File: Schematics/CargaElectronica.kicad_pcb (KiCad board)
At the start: 2 copper layers, 88 x 78.2 mm, 46 parts, among them J1 Voltage_test, J2 Voltage_IN, Q1 IRFP460, SW1 Rotary_Encoder_Switch, SW2 Btn.OK, SW3 Btn.BCK, U1 TL072, U2 Pantalla_LCD_16x2_i2c, U3 LM35-LP, U4 TL431DBZ

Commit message: Modified PCB
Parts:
- added REF**: MountingHole_3.2mm_M3_ISO14580_Pad_TopBottom, MountingHole:MountingHole_3.2mm_M3_ISO14580_Pad_TopBottom, F.Cu at (178.5, 127.8)
- added REF**: MountingHole_3.2mm_M3_ISO14580_Pad_TopBottom, MountingHole:MountingHole_3.2mm_M3_ISO14580_Pad_TopBottom, F.Cu at (104.8, 127.5)
- added REF**: MountingHole_3.2mm_M3_ISO14580_Pad_TopBottom, MountingHole:MountingHole_3.2mm_M3_ISO14580_Pad_TopBottom, F.Cu at (178.8, 97.5)
- moved REF** 13.2 mm to (126.0, 123.2)
- moved G*** 12.6 mm to (163.5, 112.2)
- moved U2 3.75 mm to (104.0, 99.8)
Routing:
- net 5V: track 89.9 -> 53.9 mm
- net Net-(A1-Pad24): track 31.2 -> 0.00 mm
- net Net-(A1-Pad23): track 27.6 -> 0.00 mm
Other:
- board size 88 x 78.2 mm -> 88 x 94.2 mm

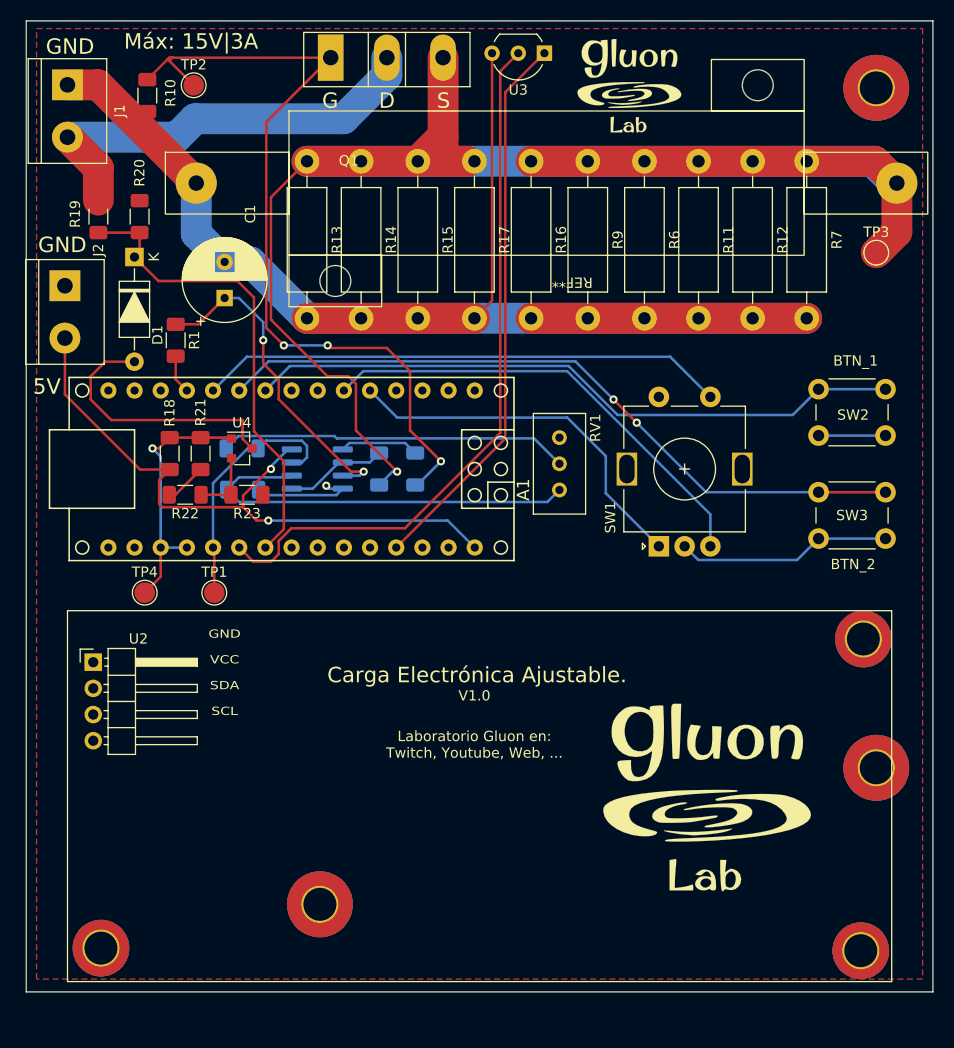
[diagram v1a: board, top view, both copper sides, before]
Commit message: Updated schematic, did not update with last commit
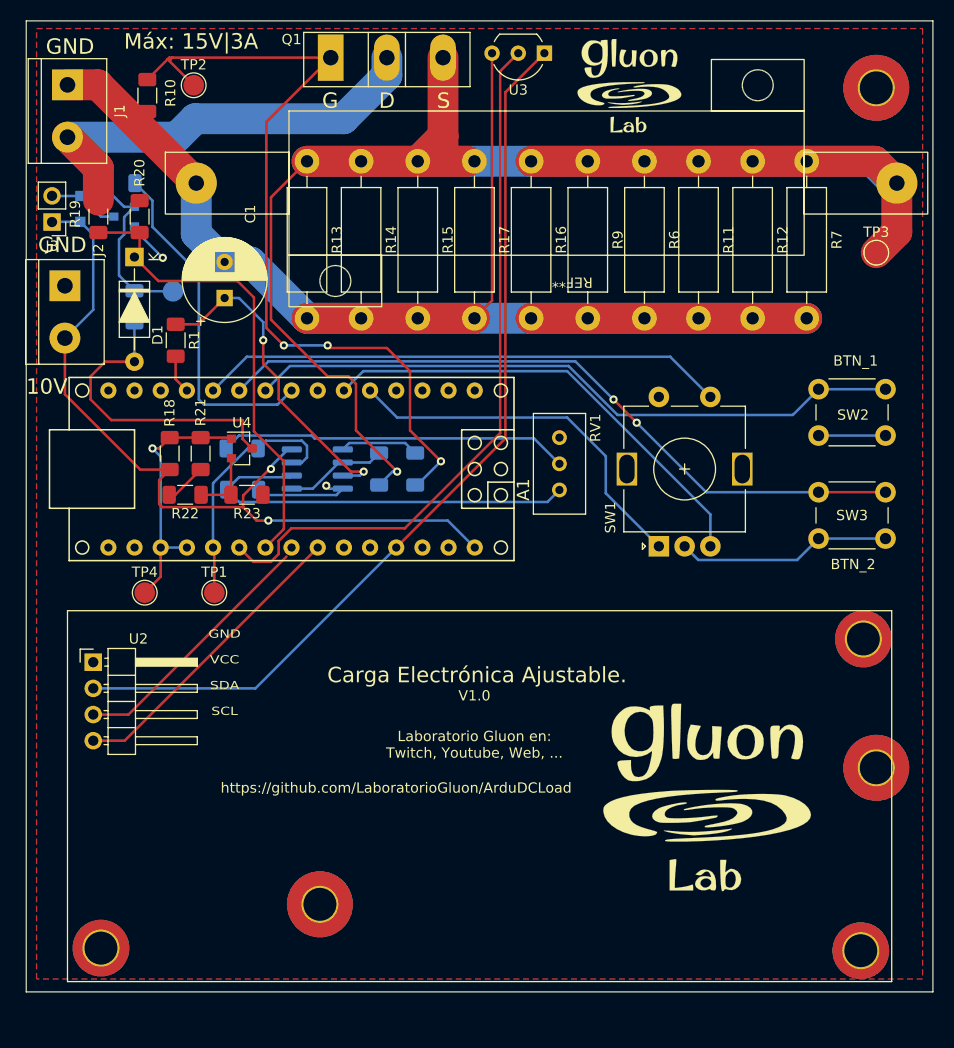
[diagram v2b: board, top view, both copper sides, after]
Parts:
- added D2: D_Schottky, Diode_SMD:D_SOD-323_HandSoldering, B.Cu at (102.8, 55.8)
- added J3: FAN_OUTPUT, Connector_PinHeader_2.54mm:PinHeader_1x02_P2.54mm_Vertical, F.Cu at (100.0, 57.0)
- added Q2: Q_NMOS_GSD, Package_TO_SOT_SMD:SOT-23, B.Cu at (107.0, 56.5)
- added R24: 1Meg, Resistor_SMD:R_1206_3216Metric_Pad1.30x1.75mm_HandSolder, B.Cu at (108.0, 65.2)
- added R3: 330, Resistor_SMD:R_1206_3216Metric_Pad1.30x1.75mm_HandSolder, B.Cu at (106.5, 53.2)
- added TP5: FanCtrl, TestPoint:TestPoint_Pad_D2.0mm, B.Cu at (111.8, 63.8)
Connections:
- A1 pad 8: unconnected-(A1-Pad8) -> FAN_CONTROL
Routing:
- net 5V: track 53.9 -> 89.0 mm
- net FAN_CONTROL: track 0.00 -> 33.3 mm
- net Net-(A1-Pad24): track 0.00 -> 29.6 mm
- net Net-(A1-Pad23): track 0.00 -> 25.1 mm
- net Net-(Q2-Pad1): track 0.00 -> 18.2 mm
- net V_IN: track 62.7 -> 78.4 mm
- net GND: track 217.5 -> 225.5 mm, vias 1 -> 2
- net Net-(J3-Pad2): track 0.00 -> 6.83 mm
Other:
- board text added: "10V"
- board text added: "https://github.com/LaboratorioGluon/ArduDCLoad"
- board text removed: "5V"

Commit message: Intermediate commit, pre-update to new kicad
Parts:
- added D3: LED, LED_THT:LED_D5.0mm_Horizontal_O1.27mm_Z3.0mm, F.Cu at (165.5, 125.2)
- added R25: 220, Resistor_SMD:R_1206_3216Metric_Pad1.30x1.75mm_HandSolder, F.Cu at (166.5, 120.0)
- moved U2 5.26 mm to (109.2, 100.0)
- moved REF** 1.25 mm to (103.5, 127.5)
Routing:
- net 5V: track 89.0 -> 128.4 mm
- net Net-(D3-Pad2): track 0.00 -> 5.25 mm
- net Net-(A1-Pad23): track 25.1 -> 26.7 mm
- net Net-(A1-Pad24): track 29.6 -> 31.1 mm

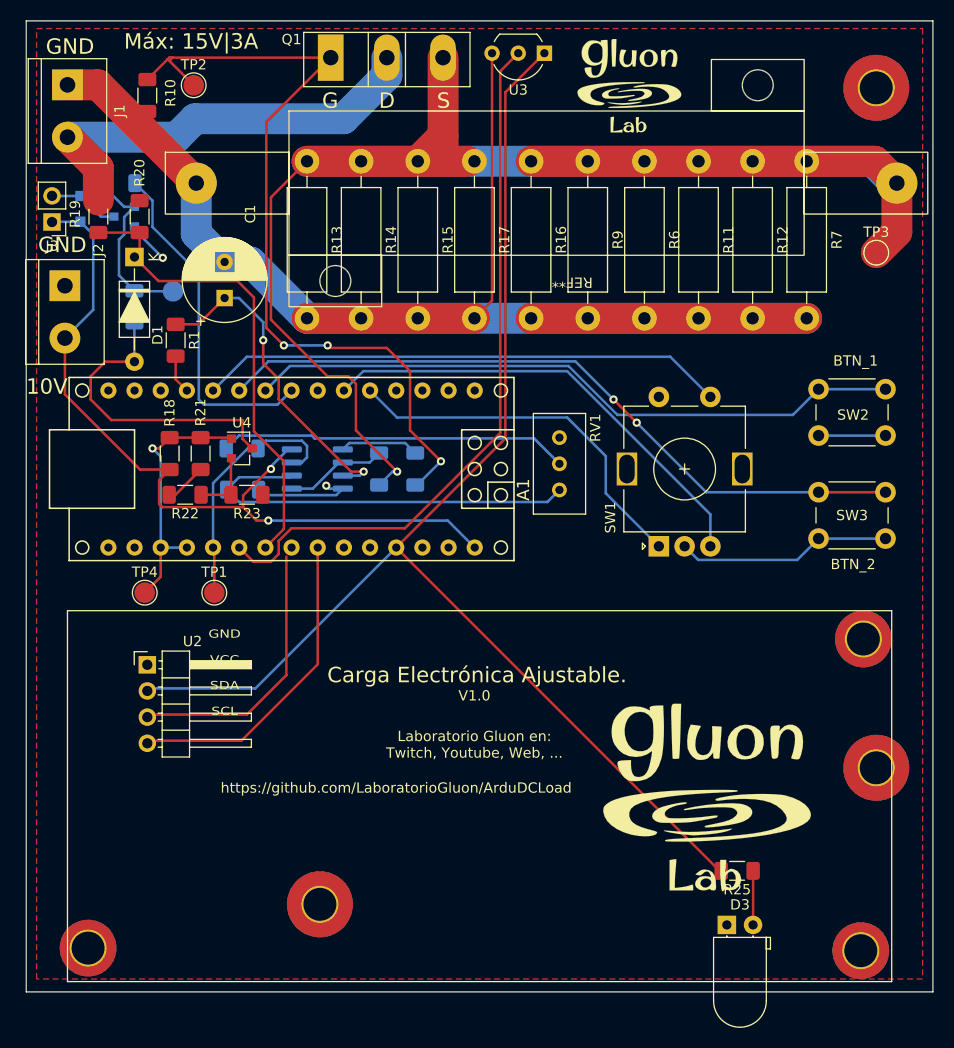
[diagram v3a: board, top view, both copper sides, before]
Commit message: Fixed errors in PCB routing
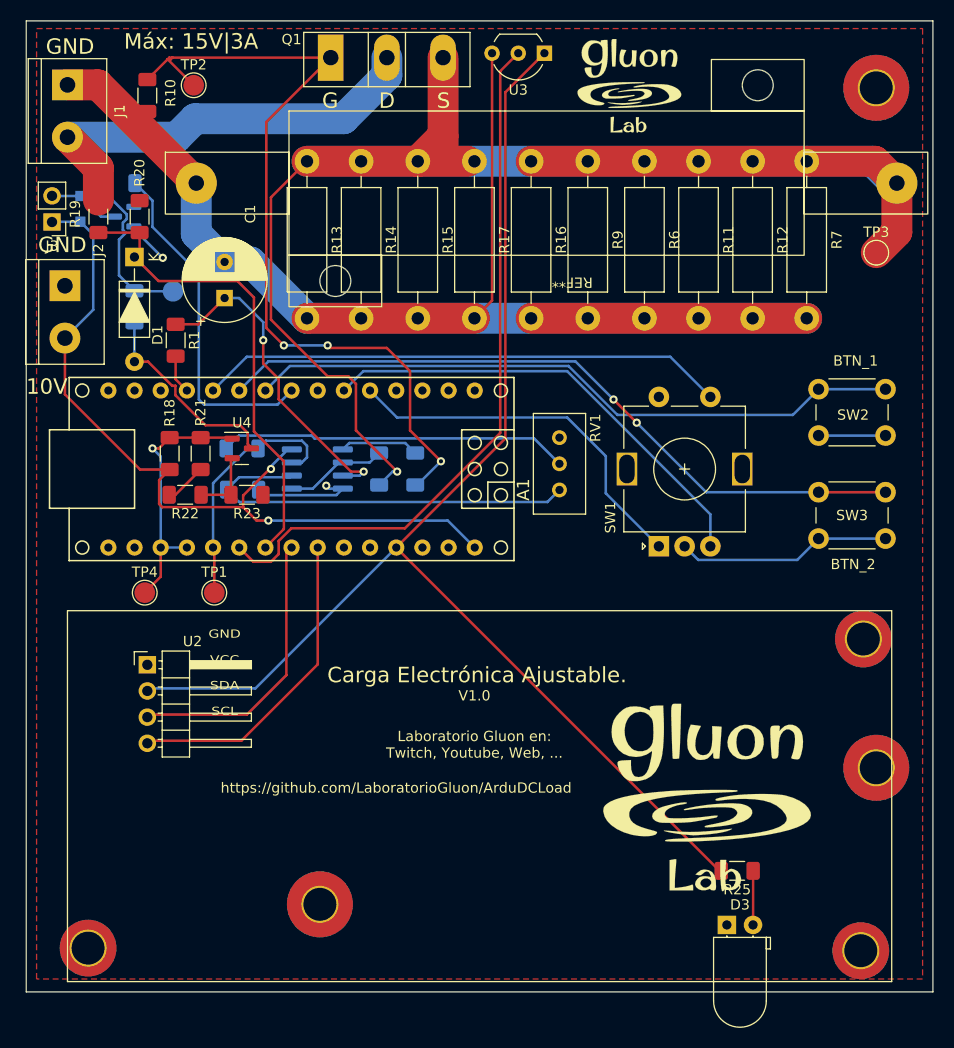
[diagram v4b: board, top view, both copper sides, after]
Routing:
- net GND: track 225.5 -> 215.8 mm
- net Net-(A1-Pad23): track 26.7 -> 27.8 mm
- net Net-(Q2-Pad1): track 18.2 -> 17.2 mm

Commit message: Intermediate commit
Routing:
- net GND: track 215.8 -> 218.6 mm, vias 2 -> 3
- net Net-(A1-Pad23): track 27.8 -> 25.6 mm
- net Net-(Q2-Pad1): track 17.2 -> 18.0 mm

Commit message: Version 1.1, fixes de la PCB
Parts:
- moved G*** 18.8 mm to (145.6, 117.9)
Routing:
- net Net-(A1-Pad23): track 25.6 -> 27.8 mm
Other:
- board text added: "V1.1"
- board text removed: "V1.0"
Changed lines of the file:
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@@
   )
   (footprint "GluonLib:LogoGluon_25mm" (layer "F.Cu")
-    (at 163.5 112.25)
+    (at 145.6 117.9)
     (attr through_hole)
     (fp_text reference "G***" (at 0 0) (layer "F.SilkS") hide
@@
     ) (layer "F.SilkS") (width 0.12) (fill solid))
   (gr_rect (start 185.5 131.75) (end 97.5 37.5) (layer "Edge.Cuts") (width 0.05) (fill none))
-  (gr_text "Laboratorio Gluon en:\nTwitch, Youtube, Web, ..." (at 141 107.75) (layer "F.SilkS")
+  (gr_text "Laboratorio Gluon en:\nTwitch, Youtube, Web, ..." (at 141.3 104) (layer "F.SilkS")
     (effects (font (size 1 1) (thickness 0.15)))
   )
@@
     (effects (font (size 0.8 1) (thickness 0.15)))
   )
-  (gr_text "https://github.com/LaboratorioGluon/ArduDCLoad" (at 133.4 111.95) (layer "F.SilkS")
+  (gr_text "https://github.com/LaboratorioGluon/ArduDCLoad" (at 140.4 107.3) (layer "F.SilkS")
     (effects (font (size 1 1) (thickness 0.15)))
   )
@@
     (effects (font (size 1.5 1.5) (thickness 0.3)))
   )
-  (gr_text "Carga Electrónica Ajustable." (at 141.25 101) (layer "F.SilkS")
+  (gr_text "Carga Electrónica Ajustable." (at 141.5 97.8) (layer "F.SilkS")
     (effects (font (size 1.5 1.5) (thickness 0.25)))
   )
-  (gr_text "V1.0" (at 141 103) (layer "F.SilkS")
+  (gr_text "V1.1" (at 141.2 100.8) (layer "F.SilkS")
     (effects (font (size 1 1) (thickness 0.15)))
   )
@@
   (segment (start 108.5 58.05) (end 108.5 59.92) (width 0.25) (layer "F.Cu") (net 9))
   (segment (start 104.5 58.05) (end 108.5 58.05) (width 0.25) (layer "F.Cu") (net 9))
+  (segment (start 109.25 105.08) (end 109.5 104.83) (width 0.25) (layer "F.Cu") (net 10))
   (segment (start 109.5 104.83) (end 118.92 104.83) (width 0.25) (layer "F.Cu") (net 10))
-  (segment (start 118.92 104.83) (end 122.75 101) (width 0.25) (layer "F.Cu") (net 10))
-  (segment (start 109.25 105.08) (end 109.5 104.83) (width 0.25) (layer "F.Cu") (net 10))
-  (segment (start 122.75 101) (end 122.9 90.6) (width 0.25) (layer "F.Cu") (net 10))
+  (segment (start 118.92 104.83) (end 123.25 100.5) (width 0.25) (layer "F.Cu") (net 10))
+  (segment (start 123.25 100.5) (end 123.25 88.62) (width 0.25) (layer "F.Cu") (net 10))
   (segment (start 118.38 107.37) (end 125.79 99.96) (width 0.25) (layer "F.Cu") (net 11))
   (segment (start 109.5 107.37) (end 118.38 107.37) (width 0.25) (layer "F.Cu") (net 11))

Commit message: Fix for PCB v1 and more sourcecode
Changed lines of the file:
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@@
     (effects (font (size 1.5 1.5) (thickness 0.3)))
   )
-  (gr_text "SCL\n" (at 116.75 104.5) (layer "F.SilkS")
+  (gr_text "SCL\n" (at 117.4 106.5) (layer "F.SilkS")
     (effects (font (size 0.8 1) (thickness 0.15)))
   )
@@
     (effects (font (size 1 1) (thickness 0.15)))
   )
-  (gr_text "VCC\n" (at 116.75 99.5) (layer "F.SilkS")
+  (gr_text "VCC\n" (at 117.4 101.5) (layer "F.SilkS")
     (effects (font (size 0.8 1) (thickness 0.15)))
   )
@@
     (effects (font (size 1 1) (thickness 0.15)))
   )
-  (gr_text "SDA" (at 116.75 102) (layer "F.SilkS")
+  (gr_text "SDA" (at 117.4 104) (layer "F.SilkS")
     (effects (font (size 0.8 1) (thickness 0.15)))
   )
@@
     (effects (font (size 1 1) (thickness 0.15)))
   )
-  (gr_text "GND" (at 116.75 97) (layer "F.SilkS")
+  (gr_text "GND" (at 117.4 99) (layer "F.SilkS")
     (effects (font (size 0.8 1) (thickness 0.15)))
   )

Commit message: Version stable
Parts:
- removed R23: 1k5, Resistor_SMD:R_1206_3216Metric_Pad1.30x1.75mm_HandSolder
- R21: value 330 -> 1k
- R22: value 2k2 -> 1k5
- R8: value 100 -> 330
- moved R22 5.60 mm to (118.5, 84.0)
- moved R21 0.10 mm to (114.4, 79.6)
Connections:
- A1 pad 29: unconnected-(A1-Pad29) -> GND
- A1 pad 4: unconnected-(A1-Pad4) -> GND
- R21 pad 1: Net-(R21-Pad1) -> Net-(U4-Pad2)
- R22 pad 1: Net-(R22-Pad1) -> GND
- R22 pad 2: Net-(R21-Pad1) -> Net-(U4-Pad2)
- U4 pad 2: Net-(R22-Pad1) -> Net-(U4-Pad2)
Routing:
- net Net-(U4-Pad2): track 0.00 -> 7.49 mm
- net Net-(R22-Pad1): track 6.47 -> 0.00 mm
- net Net-(R21-Pad1): track 4.06 -> 0.00 mm
- net GND: track 218.6 -> 217.3 mm
- net V_IN: track 78.4 -> 79.0 mm
